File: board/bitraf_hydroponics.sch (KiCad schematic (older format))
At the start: 33 parts, among them P1 12V_PWR, P10 ROT_BTN, P11 BUZZ, P12 LDR, P13 MOS_OUT_2, P14 MOS_OUT_1, P15 MOS_OUT_3, P2 I2C_1, P3 I2C_2, P4 I2C_3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

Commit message: Getting on with placing and tracing
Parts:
- added P17: BREAKOUT_1-15, Pin_Headers:Pin_Header_Straight_1x15, symbol CONN_01X15
- added P18: BREAKOUT_16-30, Pin_Headers:Pin_Header_Straight_1x15, symbol CONN_01X15
- C2, C3: footprint Capacitors_ThroughHole:C_Radial_D5_L6_P2.5 -> Capacitors_ThroughHole:C_Disc_D3_P2.5
- P13, P14, P15: footprint Pin_Headers:Pin_Header_Straight_1x02 -> Terminal_Blocks:TerminalBlock_Pheonix_MKDS1.5-2pol
- U2: footprint Power_Integrations:TO-220 -> TO_SOT_Packages_THT:TO-220_Neutral123_Vertical
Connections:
- net +12V: no longer P9.3 (P3)
- net +3V3: now also U1.1 (Vin), P17.1 (P1), P18.15 (P15)
- net +5V: now also P9.4 (P4); no longer U1.1 (Vin)
- net GND: now also P9.1 (P1), P17.2 (P2), P17.6 (P6), P18.14 (P14), P18.7 (P7); no longer P9.4 (P4)
- net LDR_PIN: now also P17.15 (P15)
- net MOS_1: now also U1.24 (D6), P18.9 (P9)
- net MOS_2: now also U1.23 (D5), P18.8 (P8)
- net MOS_3: now also U1.20 (D4), P18.5 (P5)
- net RF_DATA: now also U1.19 (D3), P18.4 (P4)
- net ROT_0: now also U1.27 (D9), P18.12 (P12)
- net ROT_1: now also U1.26 (D8), P18.11 (P11)
- net ROT_SW: now also U1.25 (D7), P18.10 (P10)
- net SCL: now also P9.3 (P3), U1.17 (D1), P18.2 (P2); no longer P9.1 (P1)
- net SDA: now also U1.18 (D2), P18.3 (P3)
- net at U1.10 (SD1): now also P17.10 (P10)
- net at U1.11 (SD2): now also P17.11 (P11)
- net at U1.12 (SD3): now also P17.12 (P12)
- net at U1.21 (3V3): now also P18.6 (P6)
- net at U1.28 (D10): now also P18.13 (P13)
- net at U1.3 (~RST): now also P17.3 (P3)
- net at U1.4 (EN): now also P17.4 (P4)
- net at U1.5 (3V3): now also P17.5 (P5)
- net at U1.7 (CLK): now also P17.7 (P7)
- net at U1.8 (SD0): now also P17.8 (P8)
- net at U1.9 (CMD): now also P17.9 (P9)
- net BUZZ_PIN renamed BUZZ
- net BUZZ: now also P18.1 (P1)
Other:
- moved on the sheet: D1, D2, D3, P10, P11, P12, P13, P14, P15, P8, P9, Q1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

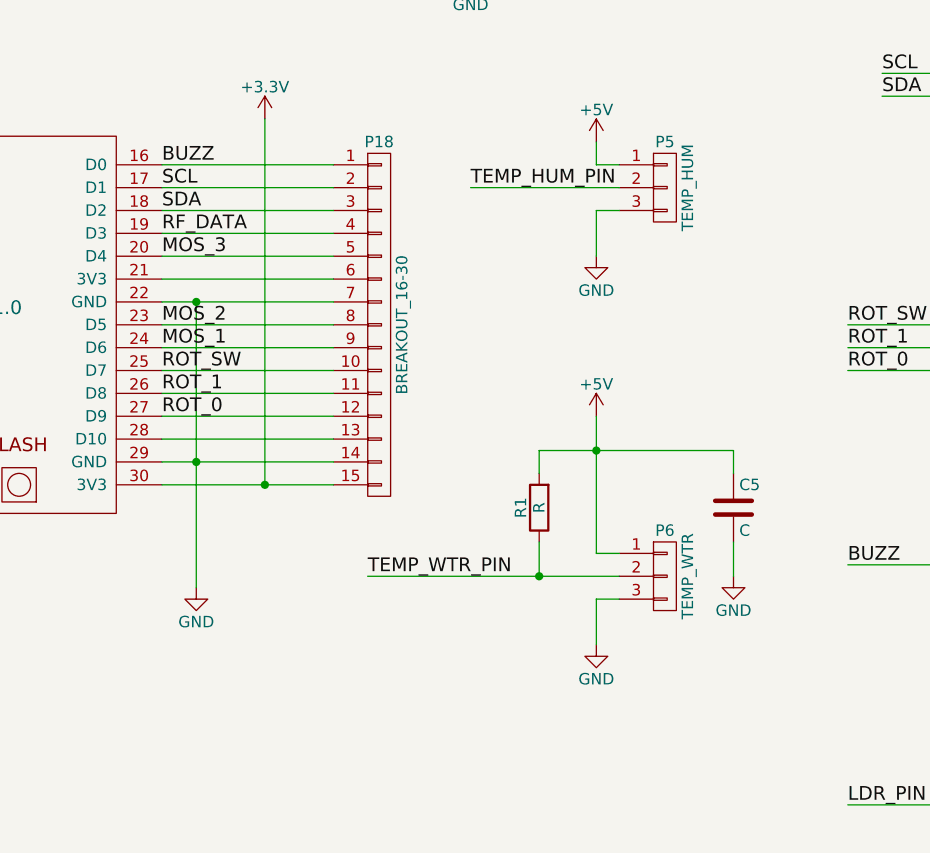
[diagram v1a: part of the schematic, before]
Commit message: Parts placed and traced. Need to define board and ground plane
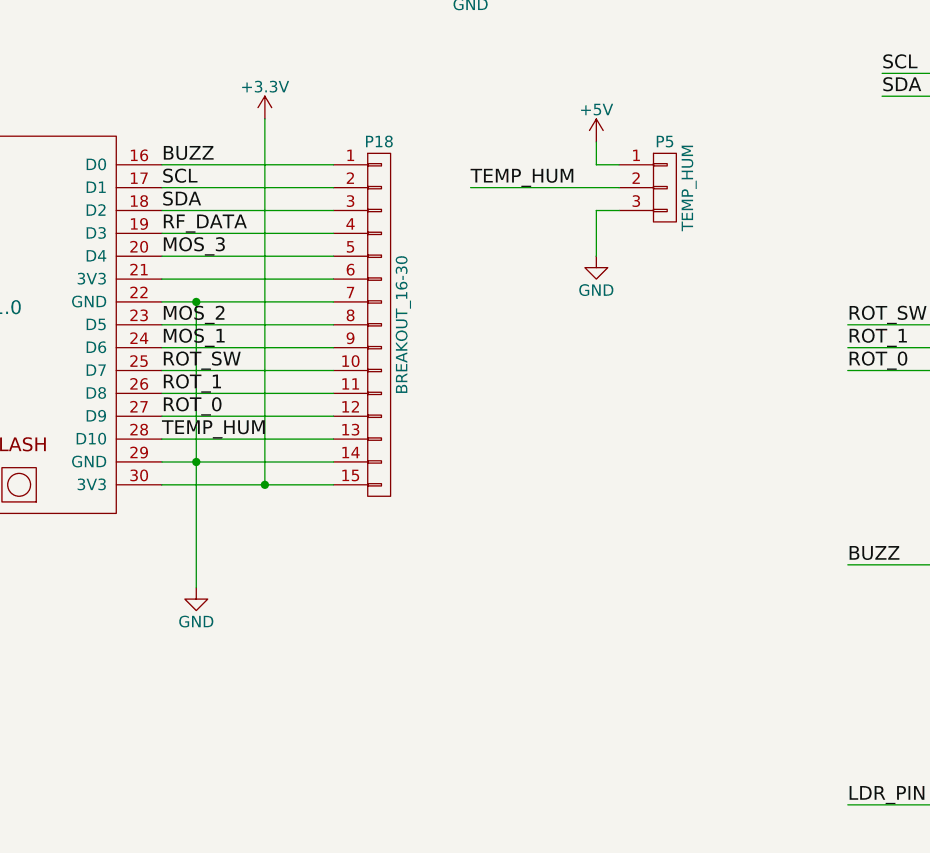
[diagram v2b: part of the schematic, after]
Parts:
- removed C5: C, Capacitors_ThroughHole:C_Radial_D5_L6_P2.5, symbol C
- removed P6: TEMP_WTR, Pin_Headers:Pin_Header_Straight_1x03, symbol CONN_01X03
- removed R1: R, Resistors_ThroughHole:Resistor_Horizontal_RM10mm, symbol R
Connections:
- net TEMP_HUM_PIN is gone; now on net TEMP_HUM: P5.2 (P2)
- net TEMP_HUM: now reaches P18.13 (P13), U1.28 (D10)
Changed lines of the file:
@@
 $EndComp
 Text Label 5350 2950 0    60   ~ 0
-TEMP_HUM_PIN
-$Comp
-L CONN_01X03 P6
-U 1 1 57E4F76D
-P 6200 4650
-F 0 "P6" H 6200 4850 50  0000 C CNN
-F 1 "TEMP_WTR" V 6300 4650 50  0000 C CNN
-F 2 "Pin_Headers:Pin_Header_Straight_1x03" H 6200 4650 50  0001 C CNN
-F 3 "" H 6200 4650 50  0000 C CNN
-	1    6200 4650
-	1    0    0    -1
-$EndComp
-Wire Wire Line
-	5900 4550 6000 4550
-Wire Wire Line
-	5900 3950 5900 4550
-$Comp
-L +5V #PWR022
-U 1 1 57E4F775
-P 5900 3950
-F 0 "#PWR022" H 5900 3800 50  0001 C CNN
-F 1 "+5V" H 5900 4090 50  0000 C CNN
-F 2 "" H 5900 3950 50  0000 C CNN
-F 3 "" H 5900 3950 50  0000 C CNN
-	1    5900 3950
-	1    0    0    -1
-$EndComp
-Wire Wire Line
-	4900 4650 6000 4650
-Wire Wire Line
-	6000 4750 5900 4750
-Wire Wire Line
-	5900 4750 5900 4950
-$Comp
-L GND #PWR023
-U 1 1 57E4F77E
-P 5900 4950
-F 0 "#PWR023" H 5900 4700 50  0001 C CNN
-F 1 "GND" H 5900 4800 50  0000 C CNN
-F 2 "" H 5900 4950 50  0000 C CNN
-F 3 "" H 5900 4950 50  0000 C CNN
-	1    5900 4950
-	1    0    0    -1
-$EndComp
-Text Label 4900 4650 0    60   ~ 0
-TEMP_WTR_PIN
-$Comp
-L R R1
-U 1 1 57E4FC46
-P 5650 4350
-F 0 "R1" V 5730 4350 50  0000 C CNN
-F 1 "R" V 5650 4350 50  0000 C CNN
-F 2 "Resistors_ThroughHole:Resistor_Horizontal_RM10mm" V 5580 4350 50  0001 C CNN
-F 3 "" H 5650 4350 50  0000 C CNN
-	1    5650 4350
-	-1   0    0    1
-$EndComp
-Wire Wire Line
-	5650 4500 5650 4650
-Connection ~ 5650 4650
-Wire Wire Line
-	5650 4200 5650 4100
-Wire Wire Line
-	5650 4100 6500 4100
-Connection ~ 5900 4100
-$Comp
-L C C5
-U 1 1 57E50696
-P 6500 4350
-F 0 "C5" H 6525 4450 50  0000 L CNN
-F 1 "C" H 6525 4250 50  0000 L CNN
-F 2 "Capacitors_ThroughHole:C_Radial_D5_L6_P2.5" H 6538 4200 50  0001 C CNN
-F 3 "" H 6500 4350 50  0000 C CNN
-	1    6500 4350
-	1    0    0    -1
-$EndComp
-Wire Wire Line
-	6500 4100 6500 4200
-Wire Wire Line
-	6500 4500 6500 4650
-$Comp
-L GND #PWR024
-U 1 1 57E50882
-P 6500 4650
-F 0 "#PWR024" H 6500 4400 50  0001 C CNN
-F 1 "GND" H 6500 4500 50  0000 C CNN
-F 2 "" H 6500 4650 50  0000 C CNN
-F 3 "" H 6500 4650 50  0000 C CNN
-	1    6500 4650
-	1    0    0    -1
-$EndComp
+TEMP_HUM
 $Comp
 L CONN_01X04 P2
@@
 Text Label 7000 4600 0    60   ~ 0
 BUZZ
+Text Label 4000 4050 0    60   ~ 0
+TEMP_HUM
 $EndSCHEMATC

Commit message: wip
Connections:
- no-connect marks 0 -> 2
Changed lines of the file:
@@
 Text Label 4000 4050 0    60   ~ 0
 TEMP_HUM
+NoConn ~ 1500 2950
+NoConn ~ 1500 3050
 $EndSCHEMATC
